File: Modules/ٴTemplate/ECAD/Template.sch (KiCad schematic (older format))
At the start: 8 parts, among them J1 comm_header, J2 prog_header, U1 ATmega328-PU

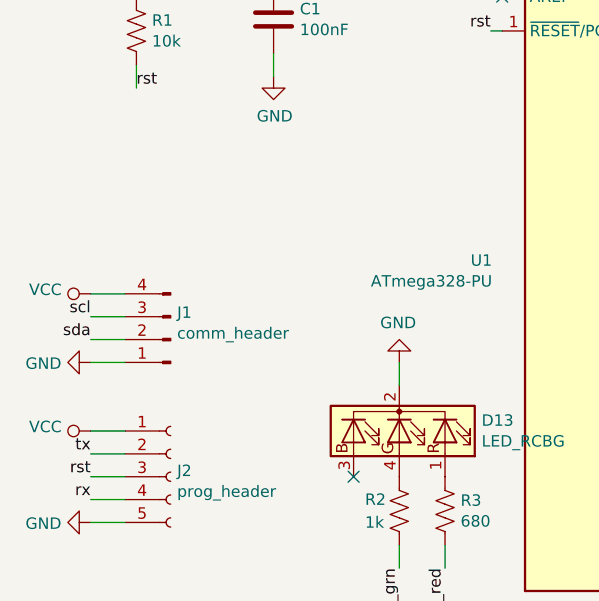
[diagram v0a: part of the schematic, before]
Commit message: Added polyfuses to all modules
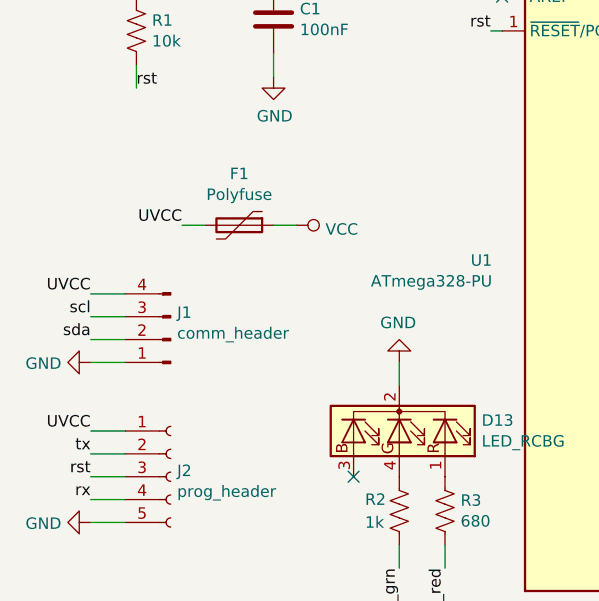
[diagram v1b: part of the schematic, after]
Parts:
- added F1: Polyfuse, symbol Device:Polyfuse
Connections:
- net VCC: now also F1.1; no longer J1.4 (Pin_4), J2.1 (Pin_1)
- new net UVCC: F1.2, J1.4 (Pin_4), J2.1 (Pin_1)
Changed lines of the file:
@@
 L power:VCC #PWR01
 U 1 1 5F5DC5B2
-P 1400 3350
-F 0 "#PWR01" H 1400 3200 50  0001 C CNN
-F 1 "VCC" V 1418 3477 50  0000 L CNN
-F 2 "" H 1400 3350 50  0001 C CNN
-F 3 "" H 1400 3350 50  0001 C CNN
-	1    1400 3350
-	0    -1   -1   0
-$EndComp
-$Comp
-L power:VCC #PWR03
-U 1 1 5F5DD568
-P 1400 3950
-F 0 "#PWR03" H 1400 3800 50  0001 C CNN
-F 1 "VCC" V 1418 4077 50  0000 L CNN
-F 2 "" H 1400 3950 50  0001 C CNN
-F 3 "" H 1400 3950 50  0001 C CNN
-	1    1400 3950
-	0    -1   -1   0
+P 2300 3050
+F 0 "#PWR01" H 2300 2900 50  0001 C CNN
+F 1 "VCC" V 2318 3177 50  0000 L CNN
+F 2 "" H 2300 3050 50  0001 C CNN
+F 3 "" H 2300 3050 50  0001 C CNN
+	1    2300 3050
+	0    1    1    0
 $EndComp
 $Comp
@@
 	1    0    0    -1
 $EndComp
+$Comp
+L Device:Polyfuse F1
+U 1 1 5F91F46D
+P 2050 3050
+F 0 "F1" V 1825 3050 50  0000 C CNN
+F 1 "Polyfuse" V 1916 3050 50  0000 C CNN
+F 2 "" H 2100 2850 50  0001 L CNN
+F 3 "~" H 2050 3050 50  0001 C CNN
+	1    2050 3050
+	0    1    1    0
+$EndComp
+Text Label 1400 3350 2    50   ~ 0
+UVCC
+Text Label 1400 3950 2    50   ~ 0
+UVCC
+Text Label 1800 3050 2    50   ~ 0
+UVCC
+Wire Wire Line
+	1800 3050 1900 3050
+Wire Wire Line
+	2200 3050 2300 3050
 $EndSCHEMATC
